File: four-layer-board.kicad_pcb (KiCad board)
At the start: 4 copper layers, 50 x 50 mm, 63 parts, among them J1 USB_B_Micro, J2 SWD Connector, J3 PWR, J4 Conn_01x06, J5 Conn_01x06, Q1 AO3401A, SW1 B3U-1000P, U1 STM32F103C8T6, U2 AMS1117-3.3, U3 USBLC6-2SC6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

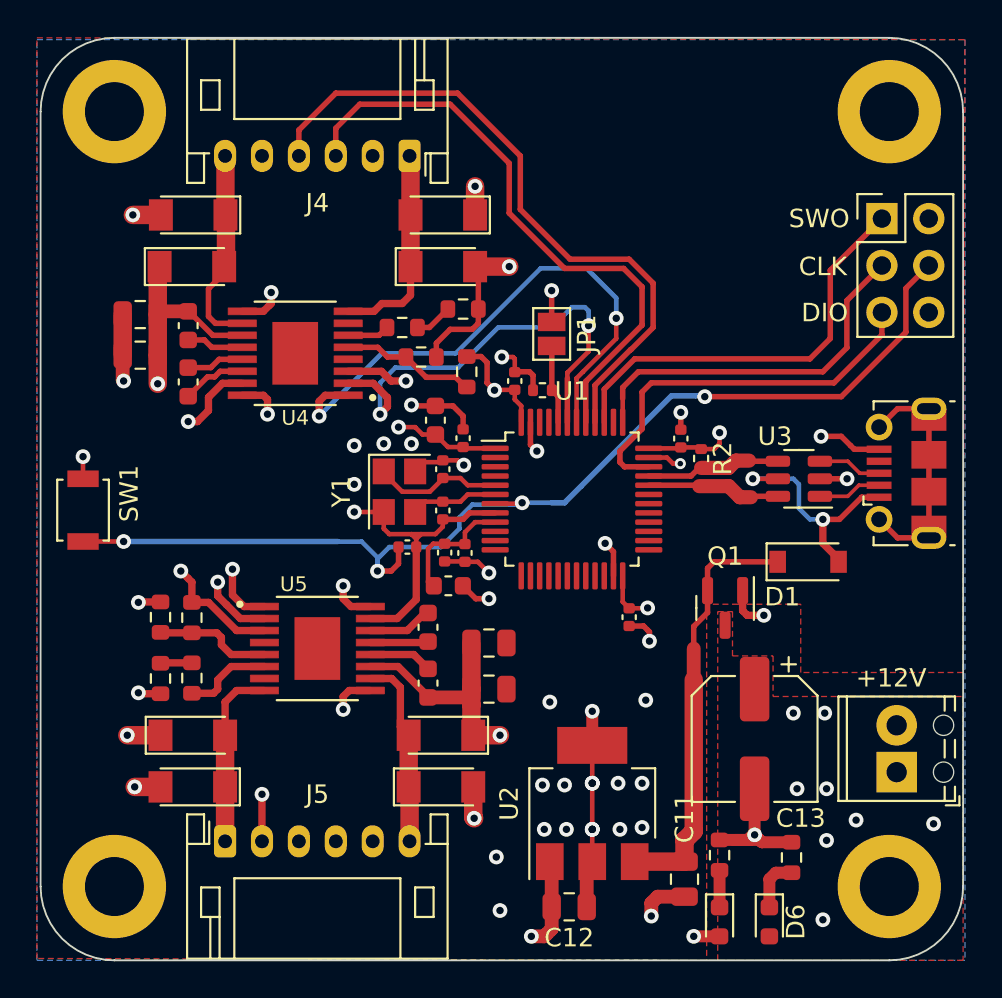
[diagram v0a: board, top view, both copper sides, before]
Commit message: Added connections for motor 2
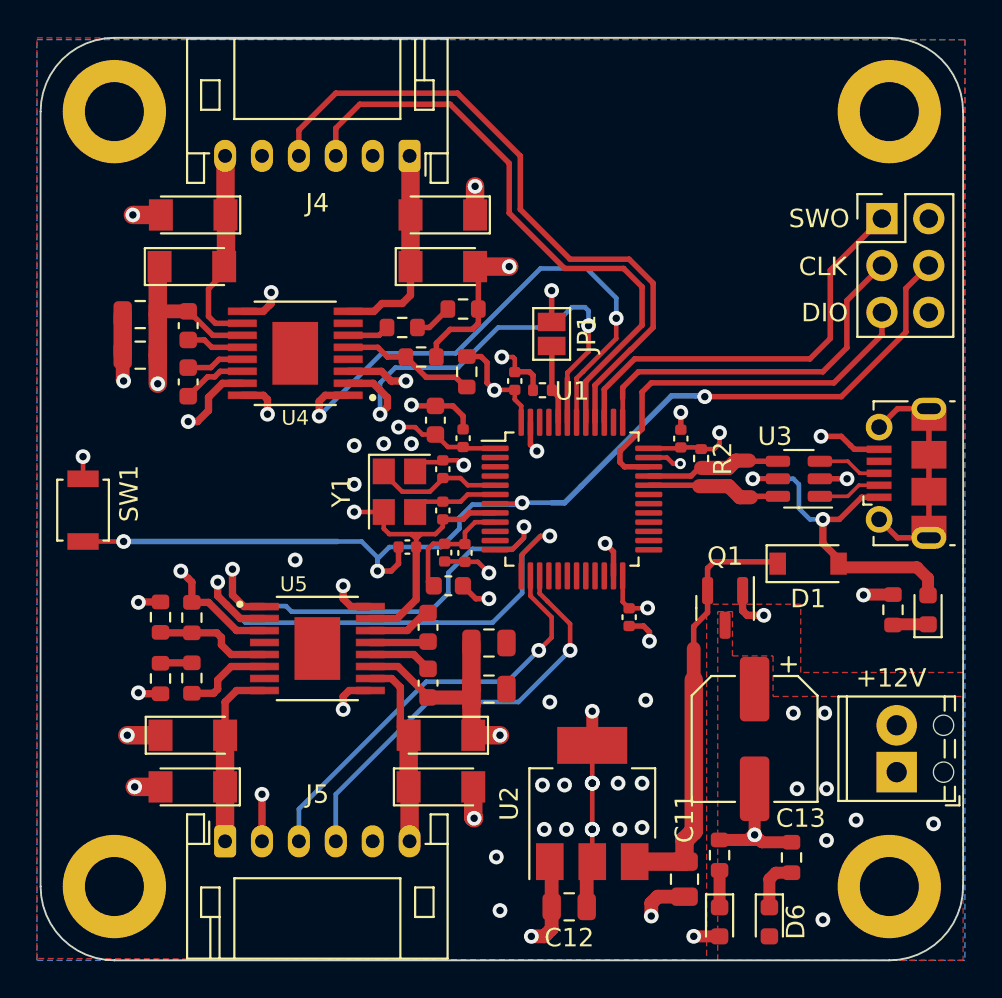
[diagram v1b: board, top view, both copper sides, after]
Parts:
- added D12: green, LED_SMD:LED_0603_1608Metric, F.Cu at (178.1, 121.0)
- added R13: 1k, Resistor_SMD:R_0603_1608Metric, F.Cu at (176.2, 121.0)
- C2: value 4u7 -> 0u1
- moved D1 0.10 mm to (171.6, 118.5)
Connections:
- J5 pad 3: /Motor Driver/M2_ENCA -> /Microcontroller/M2_ENCA
- J5 pad 4: /Motor Driver/M2_ENCB -> /Microcontroller/M2_ENCB
- U1 pad 12: unconnected-(U1-Pad12) -> /Motor Driver/M2_IN1
- U1 pad 13: unconnected-(U1-Pad13) -> /Motor Driver/M2_IN2
- U1 pad 14: unconnected-(U1-Pad14) -> /Microcontroller/M2_ENCA
- U1 pad 15: unconnected-(U1-Pad15) -> /Microcontroller/M2_ENCB
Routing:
- net /Motor Driver/M2_IN2: track 3.79 -> 29.6 mm, vias 1 -> 2
- net /Microcontroller/M2_ENCB: track 0.00 -> 23.2 mm, vias 0 -> 1
- net /Microcontroller/M2_ENCA: track 0.00 -> 23.1 mm, vias 0 -> 1
- net /Motor Driver/M2_IN1: track 3.39 -> 26.3 mm, vias 1 -> 2
- net VBUS: track 13.0 -> 19.2 mm
- net Net-(D12-Pad1): track 0.00 -> 1.92 mm
- net GND: track 90.2 -> 91.8 mm, vias 35 -> 37
